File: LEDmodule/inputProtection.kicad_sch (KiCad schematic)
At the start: 0 parts

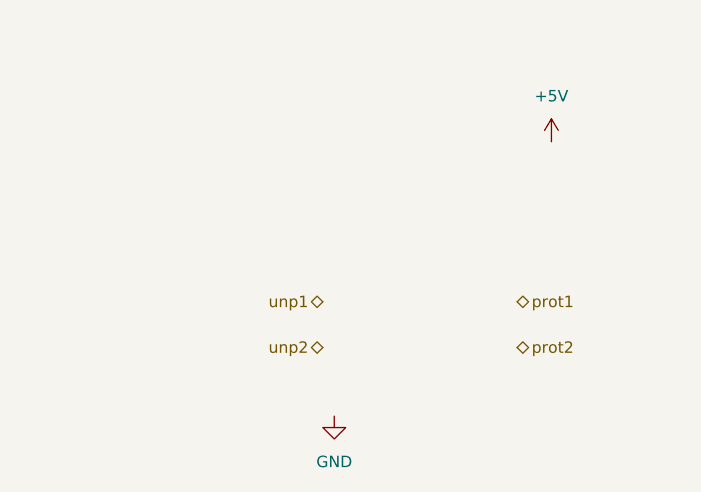
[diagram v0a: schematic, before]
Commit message: Add the input protection circuit to the schematic
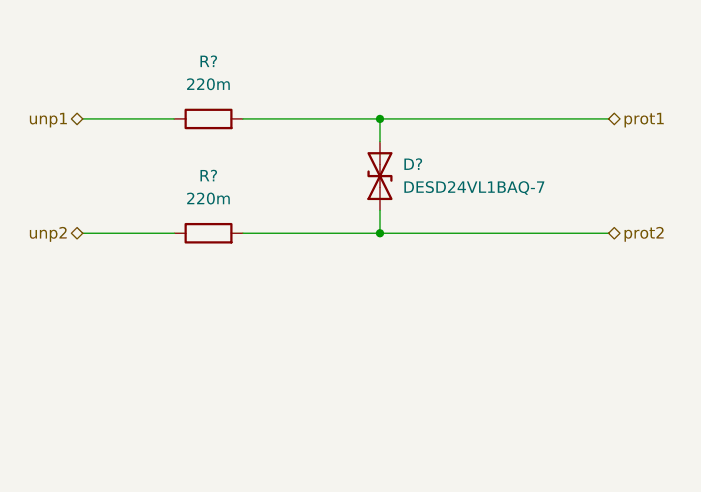
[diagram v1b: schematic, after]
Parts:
- added D?: DESD24VL1BAQ-7, symbol Device:D_TVS
- added R? (x2): 220m, symbol Device:R
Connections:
- net prot1: now also D?.2 (A2), R?.2
- net prot2: now also D?.1 (A1), R?.2
- net unp1: now also R?.1
- net unp2: now also R?.1

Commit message: Add start of comm's
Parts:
- D7: renamed from D?; now not fitted
- gave numbers to parts that had none: 2
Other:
- note added: "pulse proof"
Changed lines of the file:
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@@
 		(comment 1 "${Designed By}")
+	)
+	(text "pulse proof"
+		(exclude_from_sim no)
+		(at 82.296 41.148 0)
+		(effects
+			(font
+				(size 1.27 1.27)
+			)
+		)
 	)
 	(junction
@@
 		)
 	)
+	(polyline
+		(pts
+			(xy 76.2 64.77) (xy 76.2 66.04)
+		)
+		(stroke
+			(width 0)
+			(type default)
+		)
+	)
 	(wire
 		(pts
@@
 		)
 	)
+	(polyline
+		(pts
+			(xy 76.2 43.18) (xy 76.2 64.77)
+		)
+		(stroke
+			(width 0)
+			(type dot)
+		)
+	)
+	(polyline
+		(pts
+			(xy 76.2 66.04) (xy 88.9 66.04)
+		)
+		(stroke
+			(width 0)
+			(type default)
+		)
+	)
+	(polyline
+		(pts
+			(xy 88.9 43.18) (xy 88.9 41.91)
+		)
+		(stroke
+			(width 0)
+			(type default)
+		)
+	)
+	(polyline
+		(pts
+			(xy 88.9 41.91) (xy 76.2 41.91)
+		)
+		(stroke
+			(width 0)
+			(type default)
+		)
+	)
+	(polyline
+		(pts
+			(xy 76.2 41.91) (xy 76.2 43.18)
+		)
+		(stroke
+			(width 0)
+			(type default)
+		)
+	)
+	(polyline
+		(pts
+			(xy 88.9 66.04) (xy 88.9 64.77)
+		)
+		(stroke
+			(width 0)
+			(type default)
+		)
+	)
 	(wire
 		(pts
@@
 			(width 0)
 			(type default)
+		)
+	)
+	(polyline
+		(pts
+			(xy 88.9 43.18) (xy 88.9 64.77)
+		)
+		(stroke
+			(width 0)
+			(type dot)
 		)
 	)
@@
 		(on_board yes)
 		(dnp no)
-		(property "Reference" "R?"
+		(property "Reference" "R"
 			(at 82.55 44.45 90)
 			(effects
@@
 		)
 		(instances
-			(project ""
-				(path "/80a08b48-2579-42cd-b65f-533f20aa7c1b/3efb1bee-6b1f-4b36-9b32-ee6b0c8a5df5"
-					(reference "R?")
-					(unit 1)
-				)
-				(path "/80a08b48-2579-42cd-b65f-533f20aa7c1b/de30fabf-10e9-42a9-b2ba-3955a129919c"
-					(reference "R?")
+			(project "LEDmodule"
+				(path "/80a08b48-2579-42cd-b65f-533f20aa7c1b/d8bd32c1-f910-4768-9cf7-baf1358c7526"
+					(reference "R8")
 					(unit 1)
 				)
@@
 		(instances
 			(project "LEDmodule"
-				(path "/80a08b48-2579-42cd-b65f-533f20aa7c1b/3efb1bee-6b1f-4b36-9b32-ee6b0c8a5df5"
-					(reference "R?")
+				(path "/80a08b48-2579-42cd-b65f-533f20aa7c1b/d8bd32c1-f910-4768-9cf7-baf1358c7526"
+					(reference "R9")
 					(unit 1)
 				)
@@
 		(in_bom yes)
 		(on_board yes)
-		(dnp no)
+		(dnp yes)
 		(fields_autoplaced yes)
 		(property "Reference" "D?"
@@
 		(instances
 			(project "LEDmodule"
-				(path "/80a08b48-2579-42cd-b65f-533f20aa7c1b/3efb1bee-6b1f-4b36-9b32-ee6b0c8a5df5"
-					(reference "D?")
+				(path "/80a08b48-2579-42cd-b65f-533f20aa7c1b/d8bd32c1-f910-4768-9cf7-baf1358c7526"
+					(reference "D7")
 					(unit 1)
 				)
